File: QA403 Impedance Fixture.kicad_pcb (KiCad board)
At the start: 2 copper layers, 74.5 x 44 mm, 10 parts, among them J1 NMJ6HCD2_WITH_SCREW_TERM, J2 NMJ6HCD2_WITH_SCREW_TERM, J3 Conn_Coaxial, J4 Conn_Coaxial, J5 Conn_Coaxial, J6 Conn_Coaxial

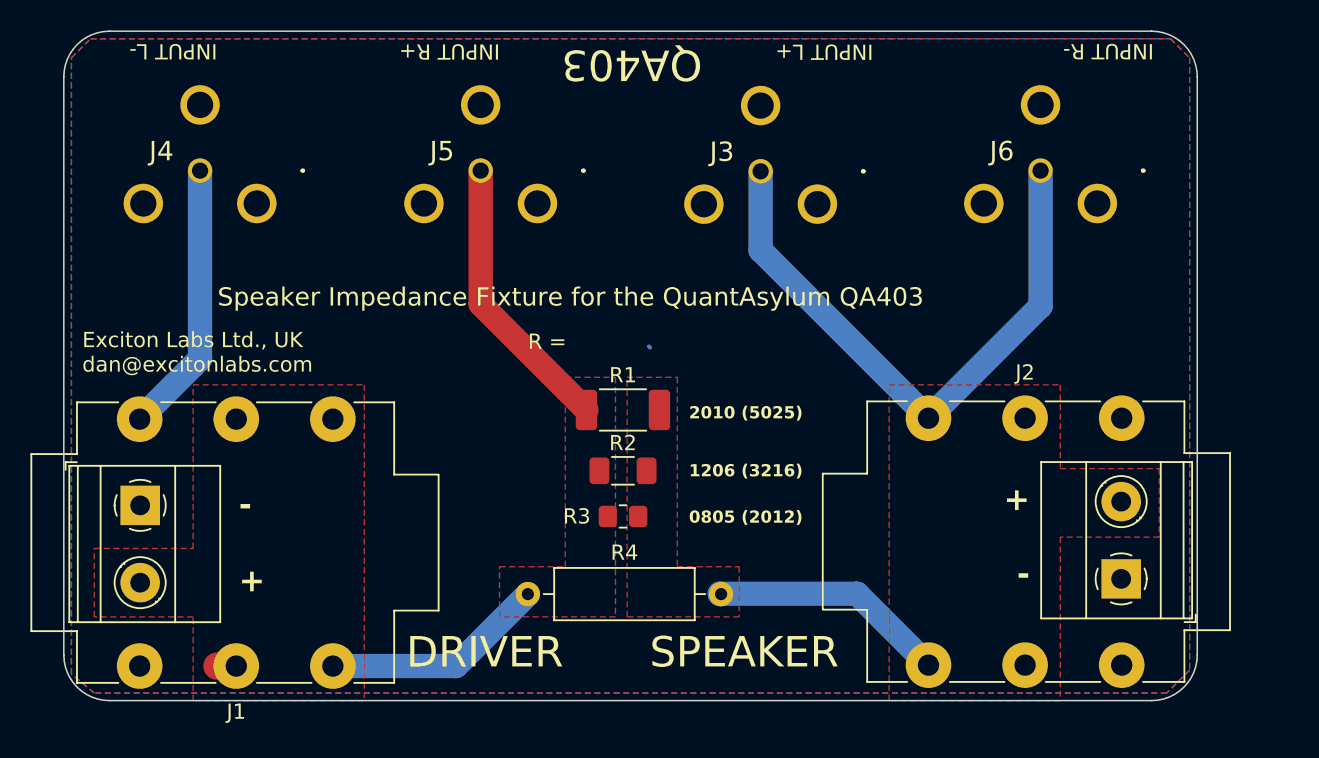
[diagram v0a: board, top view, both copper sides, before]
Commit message: Revision 2 fix error with jack socket connections
Rev 1 tied jack socket's tip and ring pins together.
This is OK if you use a stereo plug, but for will short
signal to ground when using a mono-plug. So a bug.
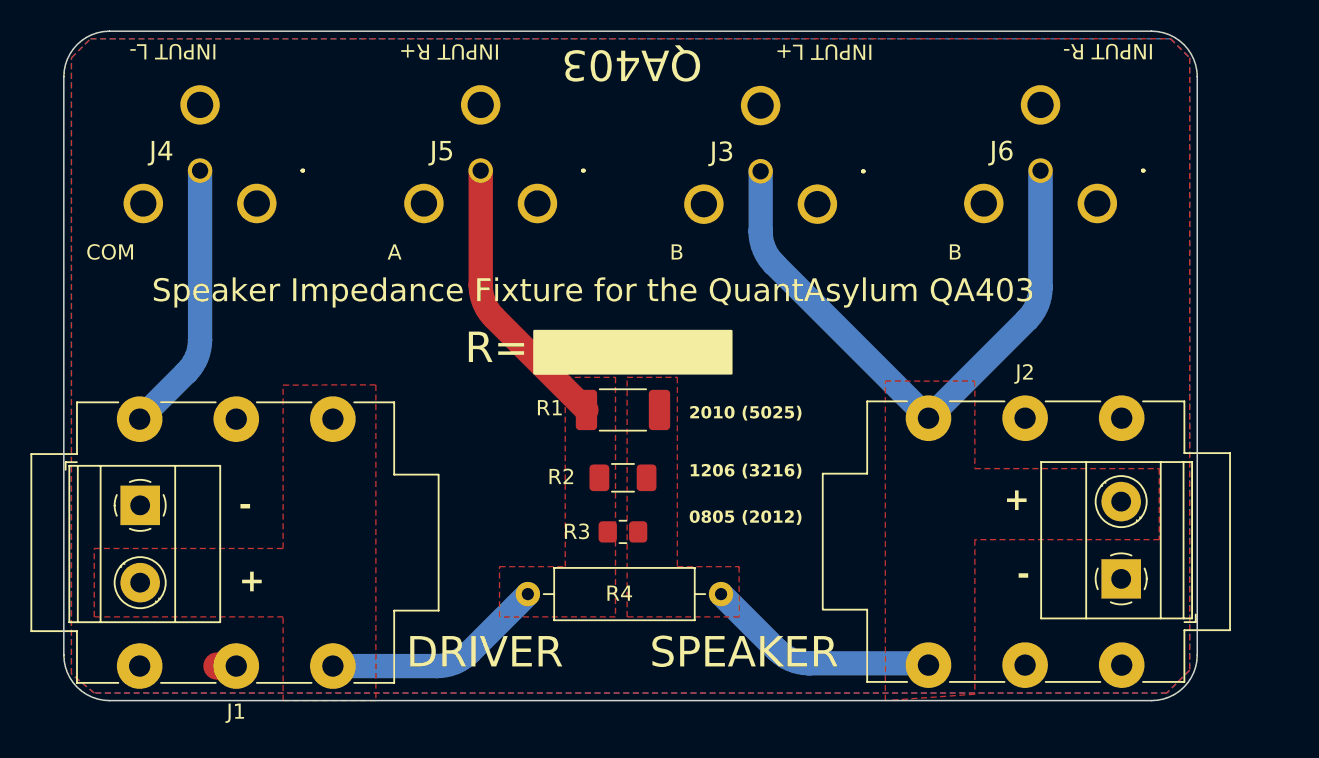
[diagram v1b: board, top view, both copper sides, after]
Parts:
- moved R3 1.02 mm to (112.3, 57.9)
- moved R2 0.46 mm to (112.3, 54.4)
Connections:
- J1 pad R: /A -> /COM
- J1 pad RN: /A -> /COM
- J2 pad R: /B -> /COM
- J2 pad RN: /B -> /COM
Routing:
- net /A: track 35.0 -> 33.5 mm
- net /COM: track 18.0 -> 19.1 mm
- net /B: track 55.9 -> 55.3 mm
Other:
- board text added: "A"
- board text added: "AMP+ AMP-"
- board text added: "B"
- board text added: "COM"
- board text added: "Connections for Impedance Measurement"
- board text added: "Designed in Cambridge; assembled in a Garage Rev 2"
- board text added: "Exciton Labs Ltd, UK dan@excitonlabs.com"
- board text added: "R"
- board text added: "R="
- board text added: "SPK+ SPK-"
- board text removed: "Designed in Cambridge; assembled in a Garage Rev 1"
- board text removed: "Exciton Labs Ltd., UK dan@excitonlabs.com"
- board text removed: "R ="
